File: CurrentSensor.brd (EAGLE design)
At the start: 100 x 26.7 mm, 20 parts, among them T1 2N3904, T2 2N3904, T3 2N3904, T4 2N3904

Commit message: Add files via upload
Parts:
- removed SW1, SW2, SW3, SW4: (no value), adafruit:TACT_PANA-EVQ
- removed U$2: BATTERY-HOLDER-2AAA, diy-modules:BATTERY-HOLDER-2AAA
- added R7: 10k, adafruit:0207/9
- C1: value (none) -> 10uf
- JP1: value (none) -> Sensor
- R2: value 10k -> 1m
- R4: value 10k -> 220
- R5: value 10k -> 4K7
- moved JP1 99.6 mm to (86.4, 20.3)
- moved T3 99.0 mm to (77.5, 20.3), turned to 270 degrees
- moved R4 96.8 mm to (58.4, 20.3)
- moved R3 93.5 mm to (67.3, 12.7)
- moved T2 93.2 mm to (77.5, 14.0), turned to 270 degrees
- moved T1 88.4 mm to (77.5, 7.62), turned to 270 degrees
- moved R2 86.1 mm to (67.3, 6.35)
- moved R5 85.9 mm to (40.6, 14.0)
- moved R6 85.2 mm to (45.7, 5.08), turned to 180 degrees
- moved LED1 69.1 mm to (68.6, 20.3)
- moved R1 67.3 mm to (85.1, 10.2), turned to 270 degrees
- moved T4 63.0 mm to (36.8, 7.62), turned to 270 degrees
- moved C1 59.9 mm to (50.8, 11.4), turned to 90 degrees
- moved D1 58.0 mm to (58.4, 16.5)
- renumbered U$1 to ESP8266-01
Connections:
- removed net N$1: SW4.P$2
- removed net N$2: U$2.BAT+
- removed net N$4: SW1.P$2
- removed net N$6: SW3.P$2
- removed net N$7: SW1.P$1, SW2.P$1, SW3.P$1, SW4.P$1, U$2.BAT-
- removed net VCC: ESP8266-01.D2
- new net /OUT: ESP8266-01.B1, R6.2, T4.1
- new net 3V3: ESP8266-01.B2, ESP8266-01.D2, R2.1, R3.1, R4.1, R6.1, R7.1
- new net N$17: ESP8266-01.C2, R7.2
- net GND: now also R5.2; no longer R1.2
- net N$10: now also R5.1; no longer R1.1
- net N$13: now also R3.2; no longer R5.2
- net N$14: now also R2.2; no longer R6.2
- net N$15: now also R1.2; no longer R3.2
- net N$3: now also R1.1; no longer R3.1
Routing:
- net N$1: track 86.2 -> 0.00 mm
- net N$4: track 76.3 -> 0.00 mm
- net N$6: track 72.2 -> 0.00 mm
- net 3V3: track 0.00 -> 65.5 mm
- net GND: track 0.00 -> 31.1 mm
- net N$10: track 0.00 -> 27.0 mm
- net /OUT: track 0.00 -> 21.4 mm
- net N$7: track 19.4 -> 0.00 mm
- net N$9: track 0.00 -> 16.1 mm
- net N$11: track 0.00 -> 8.14 mm
- net N$15: track 0.00 -> 6.56 mm
- net N$3: track 0.00 -> 6.16 mm
- net N$17: track 0.00 -> 6.00 mm
- net N$8: track 0.00 -> 5.96 mm
- net N$5: track 0.00 -> 5.88 mm
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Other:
- board size 100 x 26.7 mm -> 89.8 x 26.7 mm

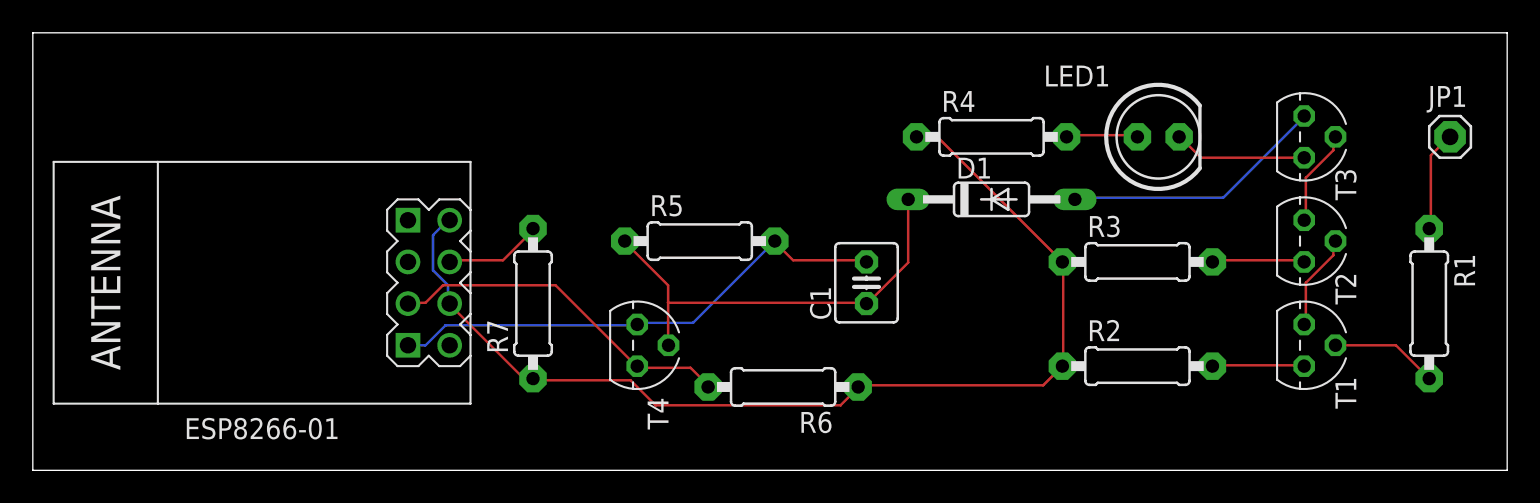
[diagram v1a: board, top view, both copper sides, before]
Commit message: Add files via upload
Added an on-board regulator.
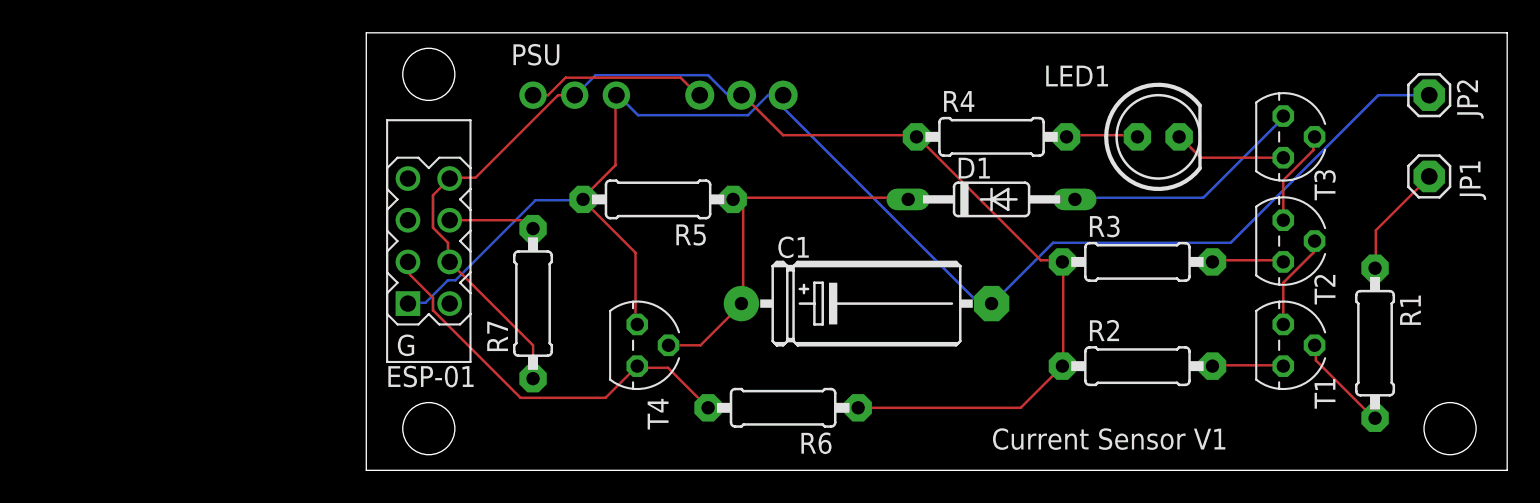
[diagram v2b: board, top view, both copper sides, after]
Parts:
- removed ESP8266-01: WIRELESS-WIFI-ESP-01, diy-modules:WIRELESS-WIFI-ESP-01
- added ESP-01: WIRELESS-WIFI-ESP-01, myParts:WIRELESS-WIFI-ESP-01
- added JP2: Gnd, adafruit:1X01
- added JP3: 3V3, adafruit:1X01-CLEANBIG
- added JP4: Vin, adafruit:1X01-CLEANBIG
- added JP5: Gnd, adafruit:1X01-CLEANBIG
- added PSU: In Out Gnd, adafruit:1X03-CLEANBIG
- C1: device adafruit:C025-040X050 -> adafruit:E15-5
- moved R1 4.09 mm to (81.8, 7.75)
- moved R5 3.59 mm to (38.1, 16.5), turned to 180 degrees
- moved JP1 2.73 mm to (85.1, 17.9)
- moved R6 1.27 mm to (45.7, 3.81)
- moved C1 1.27 mm to (50.8, 10.2), turned to 0 degrees
- moved T1 1.27 mm to (76.2, 7.62)
- moved T2 1.27 mm to (76.2, 14.0)
- moved T3 1.27 mm to (76.2, 20.3)
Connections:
- new net N$1: JP4.1, PSU.1
- net /OUT: now also ESP-01.B1; no longer ESP8266-01.B1
- net 3V3: now also ESP-01.B2, ESP-01.D2, JP3.1, PSU.2; no longer ESP8266-01.B2, ESP8266-01.D2
- net GND: now also C1.-, ESP-01.A1, JP2.1, JP5.1, PSU.3; no longer C1.2, ESP8266-01.A1
- net N$10: now also C1.+; no longer C1.1
- net N$17: now also ESP-01.C2; no longer ESP8266-01.C2
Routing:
- net GND: track 31.1 -> 91.1 mm
- net 3V3: track 65.5 -> 79.7 mm
- net N$1: track 0.00 -> 11.0 mm
- net N$10: track 27.0 -> 23.5 mm
- net /OUT: track 21.4 -> 24.4 mm
- net N$11: track 8.14 -> 6.87 mm
- net N$14: track 5.63 -> 4.39 mm
- net N$9: track 16.1 -> 14.9 mm
- net N$13: track 5.71 -> 4.48 mm
- net N$3: track 6.16 -> 6.96 mm
- net N$17: track 6.00 -> 5.32 mm
- net N$15: track 6.56 -> 6.05 mm
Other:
- board size 89.8 x 26.7 mm -> 69.5 x 26.7 mm
- board text added: "Current Sensor V1"
